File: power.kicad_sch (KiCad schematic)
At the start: 23 parts, among them Q1 DMP6050SSD, U2 171030601

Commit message: MPN and manufacturer fields for all Wuerth parts
D1, D2, J1, J2, J3, U2: added MPN and Manufacturer; D2 also got its
datasheet link (generic D_TVS symbol). All 19 Wuerth parts now carry
MPN, manufacturer and datasheet link for the BOM.

Co-Authored-By: Claude Opus 5.5 <noreply@anthropic.com>
Claude-Session: https://claude.ai/code/session_014h8cGi8SRWthYdGFH1Qgzz
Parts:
- D2: MPN (none) -> 824551241; Manufacturer (none) -> Wurth Elektronik
- U2: MPN (none) -> 171030601; Manufacturer (none) -> Wurth Elektronik
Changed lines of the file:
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@@
 			)
 		)
-		(property "Datasheet" ""
+		(property "Datasheet" "https://www.we-online.com/catalog/datasheet/824551241.pdf"
 			(at 50.8 116.84 0)
 			(hide yes)
@@
 			)
 		)
+    (property "MPN" "824551241" (at 50.8 116.84 0)
+      (effects (font (size 1.27 1.27)) (hide yes))
+    )
+    (property "Manufacturer" "Wurth Elektronik" (at 50.8 116.84 0)
+      (effects (font (size 1.27 1.27)) (hide yes))
+    )
 		(pin "1"
 		)
@@
 			)
 		)
-		(pin "1"
-		)
+    (property "MPN" "171030601" (at 149.86 114.3 0)
+      (effects (font (size 1.27 1.27)) (hide yes))
+    )
+    (property "Manufacturer" "Wurth Elektronik" (at 149.86 114.3 0)
+      (effects (font (size 1.27 1.27)) (hide yes))
+    )
+		(pin "1"
+		)

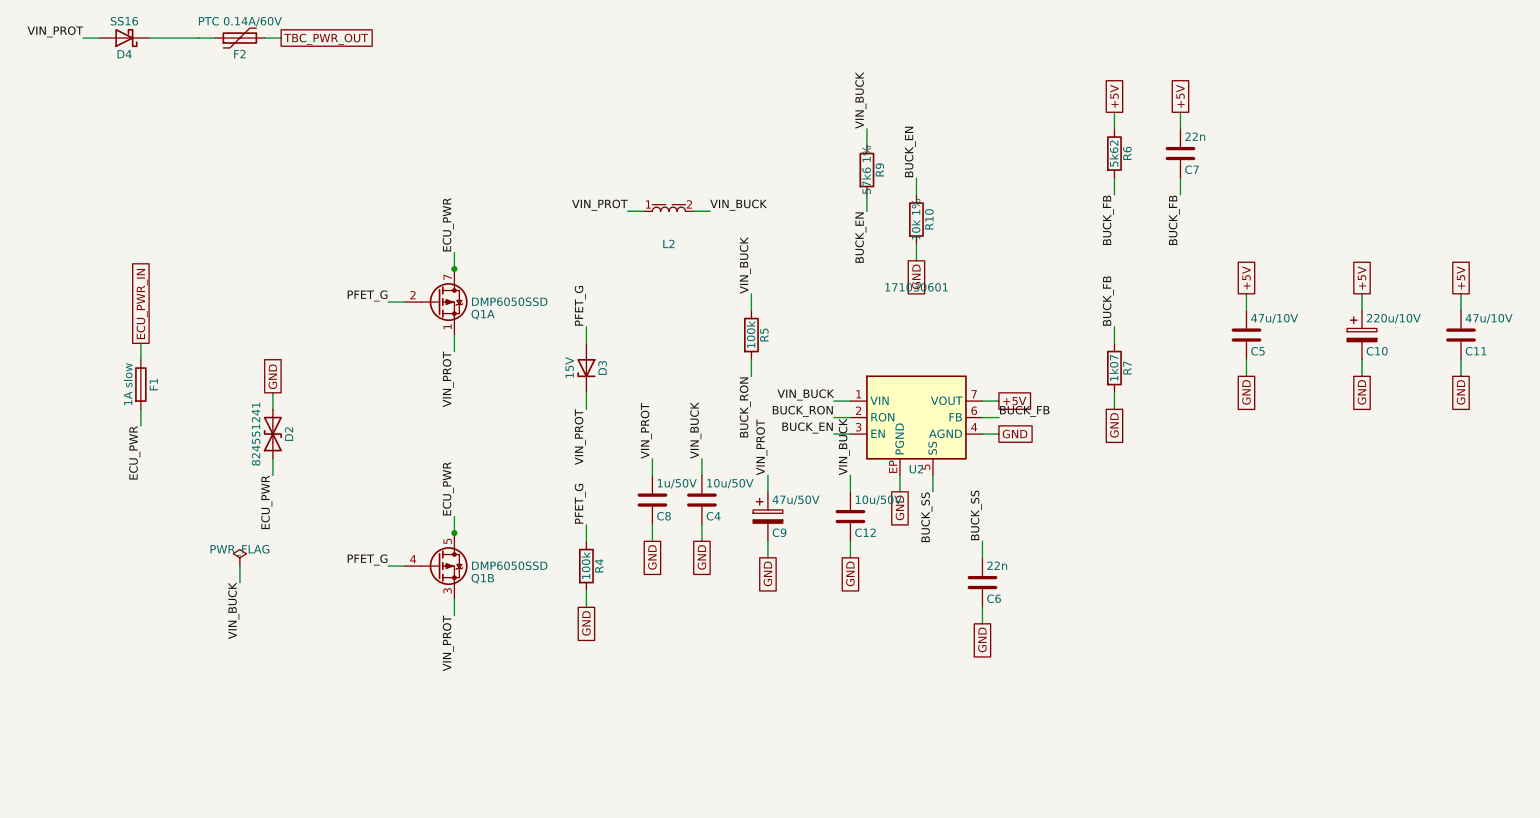
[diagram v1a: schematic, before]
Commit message: Part numbers for all remaining parts, Q1 -> Si4948BEY
- Resistors Yageo RC series 1 %. R1/R2 (split termination 750R) in
  1206 / 0.25 W: ISO 11783-2 asks for >= 125 mW for the termination
  resistors; worst case (CAN_H shorted to 24 V) is ~0.19 W each.
- D3 onsemi MMSZ5245BT1G (15 V), D4 Diodes B160-13-F (60 V Schottky)
- F1 Littelfuse 0452001.MRL NANO2 Slo-Blo 1 A / 125 V (1206 slow fuses
  are only rated 32-63 V), footprint changed to NANO2
- F2 Bourns MF-MSMF014-2 (PTC 0.14 A / 60 V, 1812)
- Q1 Vishay SI4948BEY-T1-E3 instead of the unavailable DMP6050SSD:
  dual P-ch 60 V, same SO-8 pinout (S1 G1 S2 G2 D2 D2 D1 D1), both
  halves in parallel (~60 mOhm)
- U1 Infineon TLE9250VSJXUMA1
- Every part now has MPN and manufacturer fields
- Board updated with F8 (new footprints for R1/R2/F1)

Part numbers derived from the manufacturers' naming schemes; check
availability with the Mouser BOM import before ordering.

Co-Authored-By: Claude Opus 5.5 <noreply@anthropic.com>
Claude-Session: https://claude.ai/code/session_014h8cGi8SRWthYdGFH1Qgzz
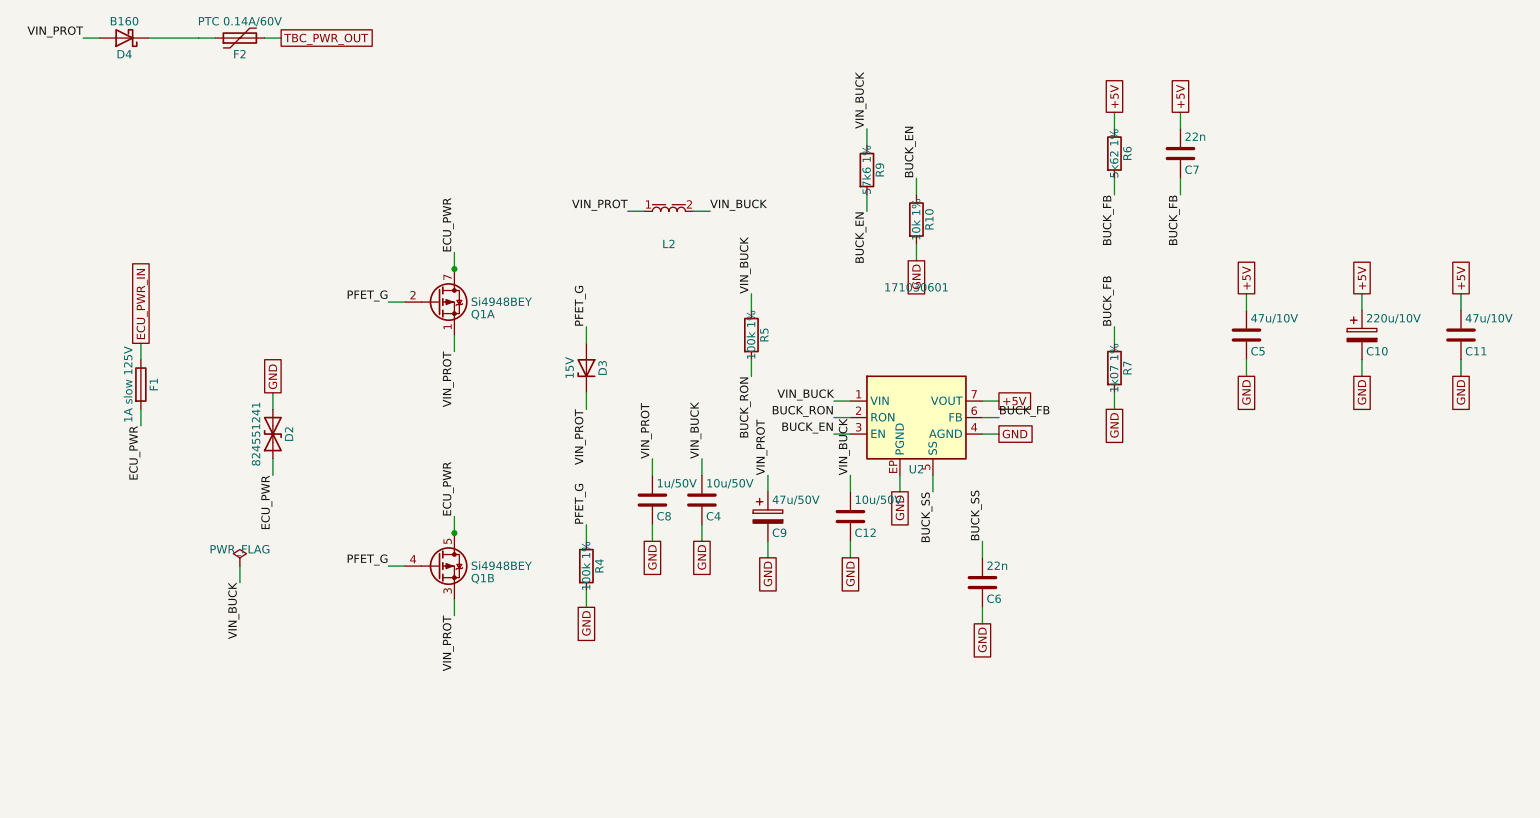
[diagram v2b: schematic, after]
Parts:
- D3: MPN (none) -> MMSZ5245BT1G; Manufacturer (none) -> onsemi
- D4: value SS16 -> B160; MPN (none) -> B160-13-F; Manufacturer (none) -> Diodes Incorporated
- F1: value 1A slow -> 1A slow 125V; footprint Fuse:Fuse_1206_3216Metric -> Fuse:Fuse_Littelfuse-NANO2-451_453; MPN (none) -> 0452001.MRL; Manufacturer (none) -> Littelfuse
- F2: MPN (none) -> MF-MSMF014-2; Manufacturer (none) -> Bourns
- Q1: value DMP6050SSD -> Si4948BEY; MPN (none) -> SI4948BEY-T1-E3; Manufacturer (none) -> Vishay
- R10: MPN (none) -> RC0603FR-0710KL; Manufacturer (none) -> Yageo
- R4, R5: value 100k -> 100k 1%; MPN (none) -> RC0603FR-07100KL; Manufacturer (none) -> Yageo
- R6: value 5k62 -> 5k62 1%; MPN (none) -> RC0603FR-075K62L; Manufacturer (none) -> Yageo
- R7: value 1k07 -> 1k07 1%; MPN (none) -> RC0603FR-071K07L; Manufacturer (none) -> Yageo
- R9: MPN (none) -> RC0603FR-0757K6L; Manufacturer (none) -> Yageo
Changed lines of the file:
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@@
 			)
 		)
-		(property "Value" "100k"
+		(property "Value" "100k 1%"
 			(at 99.06 137.16 90)
 			(show_name no)
@@
 					(size 1.27 1.27)
 				)
+			)
+		)
+		(property "Manufacturer" "Yageo"
+			(at 99.06 137.16 0)
+			(effects
+				(font
+					(size 1.27 1.27)
+				)
+				(hide yes)
+			)
+		)
+		(property "MPN" "RC0603FR-07100KL"
+			(at 99.06 137.16 0)
+			(effects
+				(font
+					(size 1.27 1.27)
+				)
+				(hide yes)
 			)
 		)
@@
 			)
 		)
-		(property "Value" "5k62"
+		(property "Value" "5k62 1%"
 			(at 180.34 73.66 90)
 			(show_name no)
@@
 					(size 1.27 1.27)
 				)
+			)
+		)
+		(property "Manufacturer" "Yageo"
+			(at 180.34 73.66 0)
+			(effects
+				(font
+					(size 1.27 1.27)
+				)
+				(hide yes)
+			)
+		)
+		(property "MPN" "RC0603FR-075K62L"
+			(at 180.34 73.66 0)
+			(effects
+				(font
+					(size 1.27 1.27)
+				)
+				(hide yes)
 			)
 		)
@@
 			)
 		)
+		(property "Manufacturer" "onsemi"
+			(at 99.06 106.68 0)
+			(effects
+				(font
+					(size 1.27 1.27)
+				)
+				(hide yes)
+			)
+		)
+		(property "MPN" "MMSZ5245BT1G"
+			(at 99.06 106.68 0)
+			(effects
+				(font
+					(size 1.27 1.27)
+				)
+				(hide yes)
+			)
+		)
 		(property "Description" "Zener diode"
 			(at 99.06 106.68 0)
@@
 			)
 		)
-		(property "Value" "DMP6050SSD"
+		(property "Value" "Si4948BEY"
 			(at 81.28 137.16 0)
 			(show_name no)
@@
 			)
 		)
-		(property "Datasheet" "https://www.diodes.com/assets/Datasheets/DMP6050SSD.pdf"
+		(property "Datasheet" "https://www.vishay.com/docs/72847/si4948be.pdf"
 			(at 81.28 133.35 0)
 			(hide yes)
@@
 				)
 				(justify left)
+			)
+		)
+		(property "Manufacturer" "Vishay"
+			(at 76.2 137.16 0)
+			(effects
+				(font
+					(size 1.27 1.27)
+				)
+				(hide yes)
+			)
+		)
+		(property "MPN" "SI4948BEY-T1-E3"
+			(at 76.2 137.16 0)
+			(effects
+				(font
+					(size 1.27 1.27)
+				)
+				(hide yes)
 			)
 		)
@@
 			)
 		)
-		(property "Value" "1k07"
+		(property "Value" "1k07 1%"
 			(at 180.34 106.68 90)
 			(show_name no)
@@
 					(size 1.27 1.27)
 				)
+			)
+		)
+		(property "Manufacturer" "Yageo"
+			(at 180.34 106.68 0)
+			(effects
+				(font
+					(size 1.27 1.27)
+				)
+				(hide yes)
+			)
+		)
+		(property "MPN" "RC0603FR-071K07L"
+			(at 180.34 106.68 0)
+			(effects
+				(font
+					(size 1.27 1.27)
+				)
+				(hide yes)
 			)
 		)
@@
 			)
 		)
-		(property "Value" "1A slow"
+		(property "Value" "1A slow 125V"
 			(at 28.575 109.22 90)
 			(show_name no)
@@
 			)
 		)
-		(property "Footprint" "Fuse:Fuse_1206_3216Metric"
+		(property "Footprint" "Fuse:Fuse_Littelfuse-NANO2-451_453"
 			(at 28.702 109.22 90)
 			(hide yes)
@@
 					(size 1.27 1.27)
 				)
+			)
+		)
+		(property "Manufacturer" "Littelfuse"
+			(at 30.48 109.22 0)
+			(effects
+				(font
+					(size 1.27 1.27)
+				)
+				(hide yes)
+			)
+		)
+		(property "MPN" "0452001.MRL"
+			(at 30.48 109.22 0)
+			(effects
+				(font
+					(size 1.27 1.27)
+				)
+				(hide yes)
 			)
 		)
@@
 			)
 		)
-		(property "Value" "100k"
+		(property "Value" "100k 1%"
 			(at 124.46 101.6 90)
 			(show_name no)
@@
 					(size 1.27 1.27)
 				)
+			)
+		)
+		(property "Manufacturer" "Yageo"
+			(at 124.46 101.6 0)
+			(effects
+				(font
+					(size 1.27 1.27)
+				)
+				(hide yes)
+			)
+		)
+		(property "MPN" "RC0603FR-07100KL"
+			(at 124.46 101.6 0)
+			(effects
+				(font
+					(size 1.27 1.27)
+				)
+				(hide yes)
 			)
 		)
@@
 			)
 		)
-		(property "Value" "DMP6050SSD"
+		(property "Value" "Si4948BEY"
 			(at 81.28 96.52 0)
 			(show_name no)
@@
 			)
 		)
-		(property "Datasheet" "https://www.diodes.com/assets/Datasheets/DMP6050SSD.pdf"
+		(property "Datasheet" "https://www.vishay.com/docs/72847/si4948be.pdf"
 			(at 81.28 92.71 0)
 			(hide yes)
@@
 				)
 				(justify left)
+			)
+		)
+		(property "Manufacturer" "Vishay"
+			(at 76.2 96.52 0)
+			(effects
+				(font
+					(size 1.27 1.27)
+				)
+				(hide yes)
+			)
+		)
+		(property "MPN" "SI4948BEY-T1-E3"
+			(at 76.2 96.52 0)
+			(effects
+				(font
+					(size 1.27 1.27)
+				)
+				(hide yes)
 			)
 		)
@@
 			)
 		)
-		(property "Value" "SS16"
+		(property "Value" "B160"
 			(at 27.94 53.34 0)
 			(show_name no)
@@
 					(size 1.27 1.27)
 				)
+			)
+		)
+		(property "Manufacturer" "Diodes Incorporated"
+			(at 27.94 55.88 0)
+			(effects
+				(font
+					(size 1.27 1.27)
+				)
+				(hide yes)
+			)
+		)
+		(property "MPN" "B160-13-F"
+			(at 27.94 55.88 0)
+			(effects
+				(font
+					(size 1.27 1.27)
+				)
+				(hide yes)
 			)
 		)
@@
 			)
 		)
+		(property "Manufacturer" "Bourns"
+			(at 45.72 55.88 0)
+			(effects
+				(font
+					(size 1.27 1.27)
+				)
+				(hide yes)
+			)
+		)
+		(property "MPN" "MF-MSMF014-2"
+			(at 45.72 55.88 0)
+			(effects
+				(font
+					(size 1.27 1.27)
+				)
+				(hide yes)
+			)
+		)
 		(property "Description" "Resettable fuse, polymeric positive temperature coefficient"
 			(at 45.72 55.88 0)
@@
 			)
 		)
+		(property "Manufacturer" "Yageo"
+			(at 142.24 76.2 0)
+			(effects
+				(font
+					(size 1.27 1.27)
+				)
+				(hide yes)
+			)
+		)
+		(property "MPN" "RC0603FR-0757K6L"
+			(at 142.24 76.2 0)
+			(effects
+				(font
+					(size 1.27 1.27)
+				)
+				(hide yes)
+			)
+		)
 		(property "Description" "Resistor"
 			(at 142.24 76.2 0)
@@
 			)
 		)
+		(property "Manufacturer" "Yageo"
+			(at 149.86 83.82 0)
+			(effects
+				(font
+					(size 1.27 1.27)
+				)
+				(hide yes)
+			)
+		)
+		(property "MPN" "RC0603FR-0710KL"
+			(at 149.86 83.82 0)
+			(effects
+				(font
+					(size 1.27 1.27)
+				)
+				(hide yes)
+			)
+		)

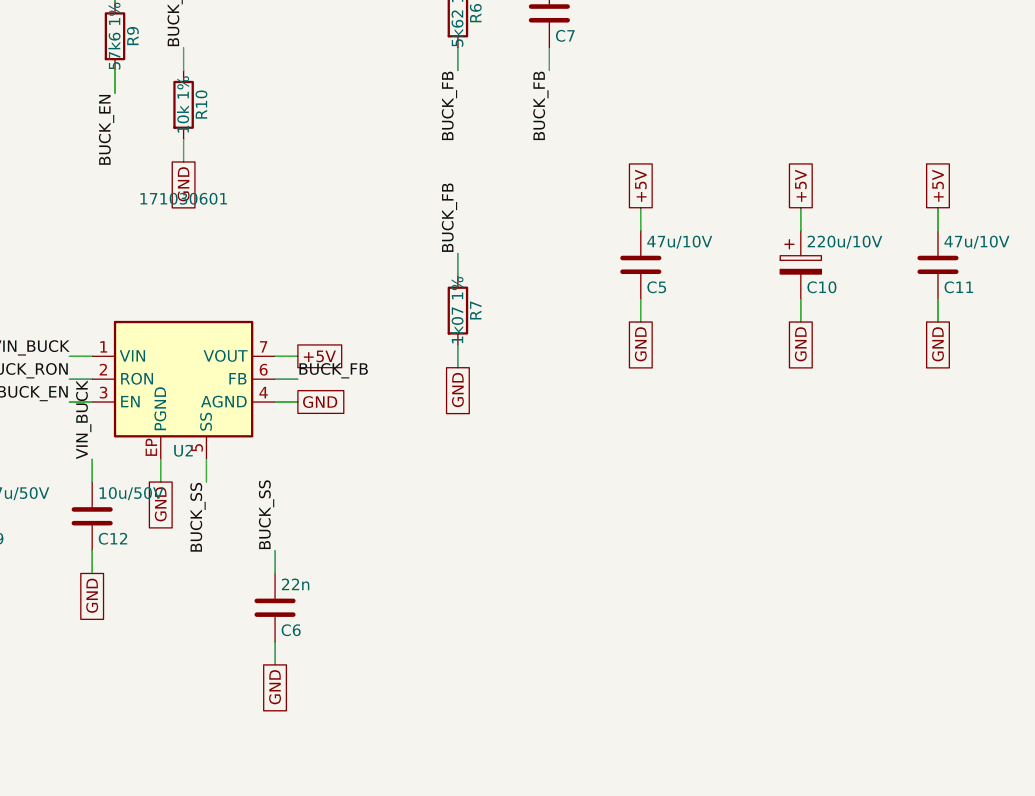
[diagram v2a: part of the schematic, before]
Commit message: Separate BUCK_AGND net, no thermal reliefs for SMD pads
- New local net BUCK_AGND on the power sheet: U2 pin 4 (AGND),
  C6 (C_SS), R7 (R_FBB), R10 (R_ENB). AGND is connected to PGND inside
  the 171030601; these grounds must be routed to the AGND pin only and
  not to the GND plane (datasheet p. 41). PWR_FLAG and a note added.
- PCB pads updated accordingly (schematic parity OK)
- All zones: pad connection "thermal reliefs for PTH only", i.e. all
  SMD pads solidly connected
- Includes placement tweaks and the VIN_BUCK zone on F.Cu done in KiCad
  (C4/C12 closer to U2, L2, C8, C9 moved)

Co-Authored-By: Claude Opus 5.5 <noreply@anthropic.com>
Claude-Session: https://claude.ai/code/session_014h8cGi8SRWthYdGFH1Qgzz
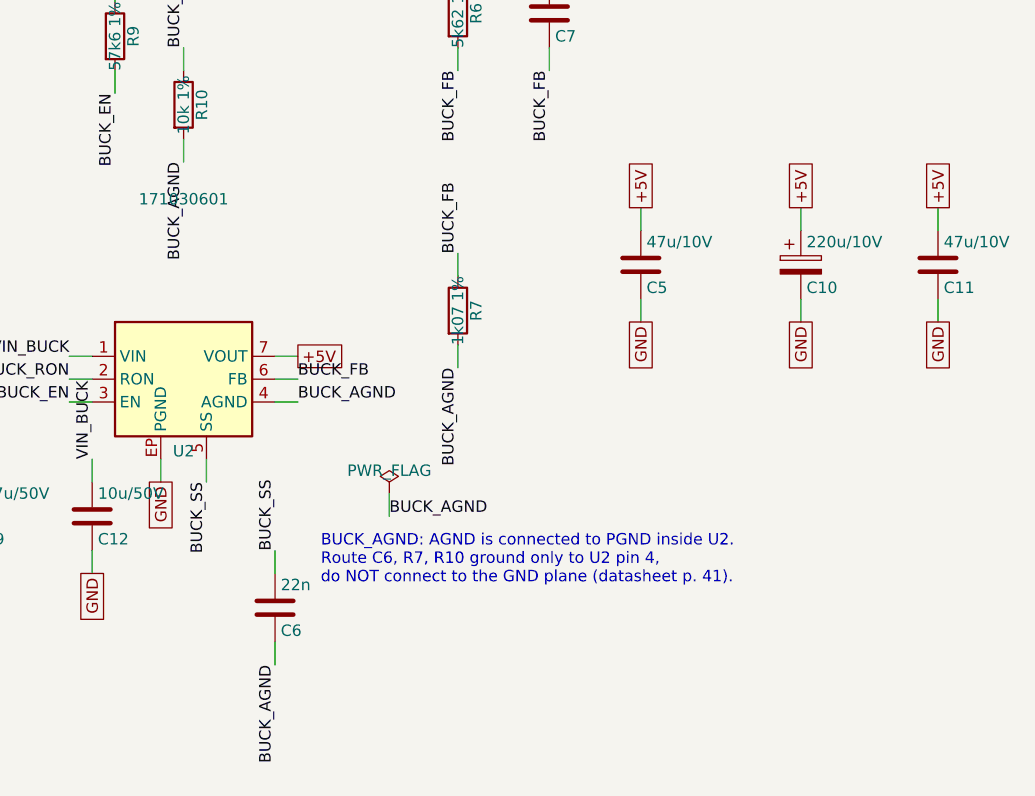
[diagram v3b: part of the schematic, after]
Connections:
- net GND: no longer C6.2, R10.2, R7.2, U2.4 (AGND)
- new net BUCK_AGND: C6.2, R10.2, R7.2, U2.4 (AGND)
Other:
- note added: "BUCK_AGND: AGND is connected to PGND inside U2. Route C6, R7, R10 ground only to U2 pin 4, do NOT connect to the GND plane (datasheet p. 41)."
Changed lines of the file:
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@@
 		)
 	)
-	(global_label "GND"
-		(shape passive)
-		(at 160.02 146.05 270)
-		(effects
-			(font
-				(size 1.27 1.27)
-			)
-			(justify right bottom)
-		)
-	)
 	(label "BUCK_RON"
 		(at 137.16 114.3 180)
@@
 		)
 	)
-	(global_label "GND"
-		(shape passive)
-		(at 180.34 113.03 270)
-		(effects
-			(font
-				(size 1.27 1.27)
-			)
-			(justify right bottom)
-		)
-	)
 	(global_label "+5V"
 		(shape passive)
@@
 		)
 	)
-	(global_label "GND"
-		(shape passive)
-		(at 162.56 116.84 0)
-		(effects
-			(font
-				(size 1.27 1.27)
-			)
-			(justify left bottom)
-		)
-	)
 	(label "BUCK_FB"
 		(at 180.34 100.33 90)
@@
 			)
 		)
-    (property "MPN" "824551241" (at 50.8 116.84 0)
-      (effects (font (size 1.27 1.27)) (hide yes))
-    )
-    (property "Manufacturer" "Wurth Elektronik" (at 50.8 116.84 0)
-      (effects (font (size 1.27 1.27)) (hide yes))
-    )
+		(property "MPN" "824551241"
+			(at 50.8 116.84 0)
+			(effects
+				(font
+					(size 1.27 1.27)
+				)
+				(hide yes)
+			)
+		)
+		(property "Manufacturer" "Wurth Elektronik"
+			(at 50.8 116.84 0)
+			(effects
+				(font
+					(size 1.27 1.27)
+				)
+				(hide yes)
+			)
+		)
 		(pin "1"
 		)
@@
 			)
 		)
-    (property "MPN" "171030601" (at 149.86 114.3 0)
-      (effects (font (size 1.27 1.27)) (hide yes))
-    )
-    (property "Manufacturer" "Wurth Elektronik" (at 149.86 114.3 0)
-      (effects (font (size 1.27 1.27)) (hide yes))
-    )
+		(property "MPN" "171030601"
+			(at 149.86 114.3 0)
+			(effects
+				(font
+					(size 1.27 1.27)
+				)
+				(hide yes)
+			)
+		)
+		(property "Manufacturer" "Wurth Elektronik"
+			(at 149.86 114.3 0)
+			(effects
+				(font
+					(size 1.27 1.27)
+				)
+				(hide yes)
+			)
+		)
 		(pin "1"
 		)
@@
 		)
 	)
-	(global_label "GND"
-		(shape passive)
+	(wire
+		(pts
+			(xy 139.7 116.84) (xy 137.16 116.84)
+		)
+		(stroke
+			(width 0)
+			(type default)
+		)
+	)
+	(label "BUCK_EN"
+		(at 137.16 116.84 180)
+		(effects
+			(font
+				(size 1.27 1.27)
+			)
+			(justify right bottom)
+		)
+	)
+	(embedded_fonts no)
+	(label "BUCK_AGND"
+		(at 162.56 116.84 0)
+		(effects
+			(font
+				(size 1.27 1.27)
+			)
+			(justify left bottom)
+		)
+	)
+	(label "BUCK_AGND"
+		(at 160.02 146.05 270)
+		(effects
+			(font
+				(size 1.27 1.27)
+			)
+			(justify right bottom)
+		)
+	)
+	(label "BUCK_AGND"
+		(at 180.34 113.03 270)
+		(effects
+			(font
+				(size 1.27 1.27)
+			)
+			(justify right bottom)
+		)
+	)
+	(label "BUCK_AGND"
 		(at 149.86 90.17 270)
 		(effects
@@
 		)
 	)
+	(symbol
+		(lib_id "power:PWR_FLAG")
+		(at 172.72 127 0)
+		(unit 1)
+		(body_style 1)
+		(exclude_from_sim no)
+		(in_bom yes)
+		(on_board yes)
+		(in_pos_files yes)
+		(dnp no)
+		(property "Reference" "#FLG04"
+			(at 172.72 128.905 0)
+			(hide yes)
+			(show_name no)
+			(do_not_autoplace no)
+			(effects
+				(font
+					(size 1.27 1.27)
+				)
+			)
+		)
+		(property "Value" "PWR_FLAG"
+			(at 172.72 124.46 0)
+			(show_name no)
+			(do_not_autoplace no)
+			(effects
+				(font
+					(size 1.27 1.27)
+				)
+			)
+		)
+		(property "Footprint" ""
+			(at 172.72 127 0)
+			(hide yes)
+			(show_name no)
+			(do_not_autoplace no)
+			(effects
+				(font
+					(size 1.27 1.27)
+				)
+			)
+		)
+		(property "Datasheet" ""
+			(at 172.72 127 0)
+			(hide yes)
+			(show_name no)
+			(do_not_autoplace no)
+			(effects
+				(font
+					(size 1.27 1.27)
+				)
+			)
+		)
+		(property "Description" "Special symbol for telling ERC where power comes from"
+			(at 172.72 127 0)
+			(hide yes)
+			(show_name no)
+			(do_not_autoplace no)
+			(effects
+				(font
+					(size 1.27 1.27)
+				)
+			)
+		)
+		(pin "1"
+		)
+		(instances
+			(project "JC8012P4A1C_I_W_Y_CAN"
+				(path "/3d717ebe-2c48-4d74-a932-f01128cae071/a2dcd761-dc69-4ab3-8065-aad2540c49d1"
+					(reference "#FLG04")
+					(unit 1)
+				)
+			)
+		)
+	)
 	(wire
 		(pts
-			(xy 139.7 116.84) (xy 137.16 116.84)
+			(xy 172.72 127.0) (xy 172.72 129.54)
 		)
 		(stroke
@@
 		)
 	)
-	(label "BUCK_EN"
-		(at 137.16 116.84 180)
+	(label "BUCK_AGND"
+		(at 172.72 129.54 0)
 		(effects
 			(font
 				(size 1.27 1.27)
 			)
-			(justify right bottom)
+			(justify left bottom)
+		)
+	)
+	(text "BUCK_AGND: AGND is connected to PGND inside U2.\nRoute C6, R7, R10 ground only to U2 pin 4,\ndo NOT connect to the GND plane (datasheet p. 41)."
+		(exclude_from_sim no)
+		(at 165.1 137.16 0)
+		(effects
+			(font
+				(size 1.27 1.27)
+			)
+			(justify left bottom)
 		)
 	)
-	(embedded_fonts no)
 )
